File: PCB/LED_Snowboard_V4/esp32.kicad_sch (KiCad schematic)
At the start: 28 parts

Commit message: makerfaire
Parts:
- TP1, TP2, TP3, TP4, TP5: footprint (none) -> TestPoint:TestPoint_Pad_3.0x3.0mm
- TP10, TP11, TP12, TP13, TP14, TP15, TP16, TP17, TP18, TP19, TP20, TP21, TP22, TP23, TP24, TP25, TP26, TP27, TP6, TP7, TP8, TP9: footprint (none) -> TestPoint:TestPoint_Pad_D1.5mm
- U1: footprint (none) -> MicroControllers:MODULE_ESP32_DEVKIT_V1
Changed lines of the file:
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@@
       (effects (font (size 1.27 1.27)))
     )
-    (property "Footprint" "" (at 31.75 181.61 0)
+    (property "Footprint" "TestPoint:TestPoint_Pad_D1.5mm" (at 31.75 181.61 0)
       (effects (font (size 1.27 1.27)) hide)
     )
@@
       (effects (font (size 1.27 1.27)))
     )
-    (property "Footprint" "" (at 31.75 34.29 0)
+    (property "Footprint" "TestPoint:TestPoint_Pad_3.0x3.0mm" (at 31.75 34.29 0)
       (effects (font (size 1.27 1.27)) hide)
     )
@@
       (effects (font (size 1.27 1.27)))
     )
-    (property "Footprint" "" (at 143.51 111.76 0)
+    (property "Footprint" "MicroControllers:MODULE_ESP32_DEVKIT_V1" (at 143.51 111.76 0)
       (effects (font (size 1.27 1.27)) hide)
     )
@@
       (effects (font (size 1.27 1.27)))
     )
-    (property "Footprint" "" (at 31.75 186.69 0)
+    (property "Footprint" "TestPoint:TestPoint_Pad_D1.5mm" (at 31.75 186.69 0)
       (effects (font (size 1.27 1.27)) hide)
     )
@@
       (effects (font (size 1.27 1.27)))
     )
-    (property "Footprint" "" (at 31.75 116.84 0)
+    (property "Footprint" "TestPoint:TestPoint_Pad_D1.5mm" (at 31.75 116.84 0)
       (effects (font (size 1.27 1.27)) hide)
     )
@@
       (effects (font (size 1.27 1.27)))
     )
-    (property "Footprint" "" (at 31.75 167.64 0)
+    (property "Footprint" "TestPoint:TestPoint_Pad_D1.5mm" (at 31.75 167.64 0)
       (effects (font (size 1.27 1.27)) hide)
     )
@@
       (effects (font (size 1.27 1.27)))
     )
-    (property "Footprint" "" (at 31.75 138.43 0)
+    (property "Footprint" "TestPoint:TestPoint_Pad_D1.5mm" (at 31.75 138.43 0)
       (effects (font (size 1.27 1.27)) hide)
     )
@@
       (effects (font (size 1.27 1.27)))
     )
-    (property "Footprint" "" (at 31.75 162.56 0)
+    (property "Footprint" "TestPoint:TestPoint_Pad_D1.5mm" (at 31.75 162.56 0)
       (effects (font (size 1.27 1.27)) hide)
     )
@@
       (effects (font (size 1.27 1.27)))
     )
-    (property "Footprint" "" (at 31.75 60.96 0)
+    (property "Footprint" "TestPoint:TestPoint_Pad_D1.5mm" (at 31.75 60.96 0)
       (effects (font (size 1.27 1.27)) hide)
     )
@@
       (effects (font (size 1.27 1.27)))
     )
-    (property "Footprint" "" (at 31.75 29.21 0)
+    (property "Footprint" "TestPoint:TestPoint_Pad_3.0x3.0mm" (at 31.75 29.21 0)
       (effects (font (size 1.27 1.27)) hide)
     )
@@
       (effects (font (size 1.27 1.27)))
     )
-    (property "Footprint" "" (at 31.75 39.37 0)
+    (property "Footprint" "TestPoint:TestPoint_Pad_3.0x3.0mm" (at 31.75 39.37 0)
       (effects (font (size 1.27 1.27)) hide)
     )
@@
       (effects (font (size 1.27 1.27)))
     )
-    (property "Footprint" "" (at 31.75 24.13 0)
+    (property "Footprint" "TestPoint:TestPoint_Pad_3.0x3.0mm" (at 31.75 24.13 0)
       (effects (font (size 1.27 1.27)) hide)
     )
@@
       (effects (font (size 1.27 1.27)))
     )
-    (property "Footprint" "" (at 31.75 133.35 0)
+    (property "Footprint" "TestPoint:TestPoint_Pad_D1.5mm" (at 31.75 133.35 0)
       (effects (font (size 1.27 1.27)) hide)
     )
@@
       (effects (font (size 1.27 1.27)))
     )
-    (property "Footprint" "" (at 31.75 105.41 0)
+    (property "Footprint" "TestPoint:TestPoint_Pad_D1.5mm" (at 31.75 105.41 0)
       (effects (font (size 1.27 1.27)) hide)
     )
@@
       (effects (font (size 1.27 1.27)))
     )
-    (property "Footprint" "" (at 31.75 86.36 0)
+    (property "Footprint" "TestPoint:TestPoint_Pad_D1.5mm" (at 31.75 86.36 0)
       (effects (font (size 1.27 1.27)) hide)
     )
@@
       (effects (font (size 1.27 1.27)))
     )
-    (property "Footprint" "" (at 31.75 76.2 0)
+    (property "Footprint" "TestPoint:TestPoint_Pad_D1.5mm" (at 31.75 76.2 0)
       (effects (font (size 1.27 1.27)) hide)
     )
@@
       (effects (font (size 1.27 1.27)))
     )
-    (property "Footprint" "" (at 31.75 100.33 0)
+    (property "Footprint" "TestPoint:TestPoint_Pad_D1.5mm" (at 31.75 100.33 0)
       (effects (font (size 1.27 1.27)) hide)
     )
@@
       (effects (font (size 1.27 1.27)))
     )
-    (property "Footprint" "" (at 31.75 50.8 0)
+    (property "Footprint" "TestPoint:TestPoint_Pad_D1.5mm" (at 31.75 50.8 0)
       (effects (font (size 1.27 1.27)) hide)
     )
@@
       (effects (font (size 1.27 1.27)))
     )
-    (property "Footprint" "" (at 31.75 157.48 0)
+    (property "Footprint" "TestPoint:TestPoint_Pad_D1.5mm" (at 31.75 157.48 0)
       (effects (font (size 1.27 1.27)) hide)
     )
@@
       (effects (font (size 1.27 1.27)))
     )
-    (property "Footprint" "" (at 31.75 19.05 0)
+    (property "Footprint" "TestPoint:TestPoint_Pad_3.0x3.0mm" (at 31.75 19.05 0)
       (effects (font (size 1.27 1.27)) hide)
     )
@@
       (effects (font (size 1.27 1.27)))
     )
-    (property "Footprint" "" (at 31.75 121.92 0)
+    (property "Footprint" "TestPoint:TestPoint_Pad_D1.5mm" (at 31.75 121.92 0)
       (effects (font (size 1.27 1.27)) hide)
     )
@@
       (effects (font (size 1.27 1.27)))
     )
-    (property "Footprint" "" (at 31.75 66.04 0)
+    (property "Footprint" "TestPoint:TestPoint_Pad_D1.5mm" (at 31.75 66.04 0)
       (effects (font (size 1.27 1.27)) hide)
     )
@@
       (effects (font (size 1.27 1.27)))
     )
-    (property "Footprint" "" (at 31.75 55.88 0)
+    (property "Footprint" "TestPoint:TestPoint_Pad_D1.5mm" (at 31.75 55.88 0)
       (effects (font (size 1.27 1.27)) hide)
     )
@@
       (effects (font (size 1.27 1.27)))
     )
-    (property "Footprint" "" (at 31.75 91.44 0)
+    (property "Footprint" "TestPoint:TestPoint_Pad_D1.5mm" (at 31.75 91.44 0)
       (effects (font (size 1.27 1.27)) hide)
     )
@@
       (effects (font (size 1.27 1.27)))
     )
-    (property "Footprint" "" (at 31.75 143.51 0)
+    (property "Footprint" "TestPoint:TestPoint_Pad_D1.5mm" (at 31.75 143.51 0)
       (effects (font (size 1.27 1.27)) hide)
     )
@@
       (effects (font (size 1.27 1.27)))
     )
-    (property "Footprint" "" (at 31.75 176.53 0)
+    (property "Footprint" "TestPoint:TestPoint_Pad_D1.5mm" (at 31.75 176.53 0)
       (effects (font (size 1.27 1.27)) hide)
     )
@@
       (effects (font (size 1.27 1.27)))
     )
-    (property "Footprint" "" (at 31.75 148.59 0)
+    (property "Footprint" "TestPoint:TestPoint_Pad_D1.5mm" (at 31.75 148.59 0)
       (effects (font (size 1.27 1.27)) hide)
     )
@@
       (effects (font (size 1.27 1.27)))
     )
-    (property "Footprint" "" (at 31.75 81.28 0)
-      (effects (font (size 1.27 1.27)) hide)
-    )
+    (property "Footprint" "TestPoint:TestPoint_Pad_D1.5mm" (at 31.75 81.28 0)
+      (effects (font (size 1.27 1.27)) hide)
+    )

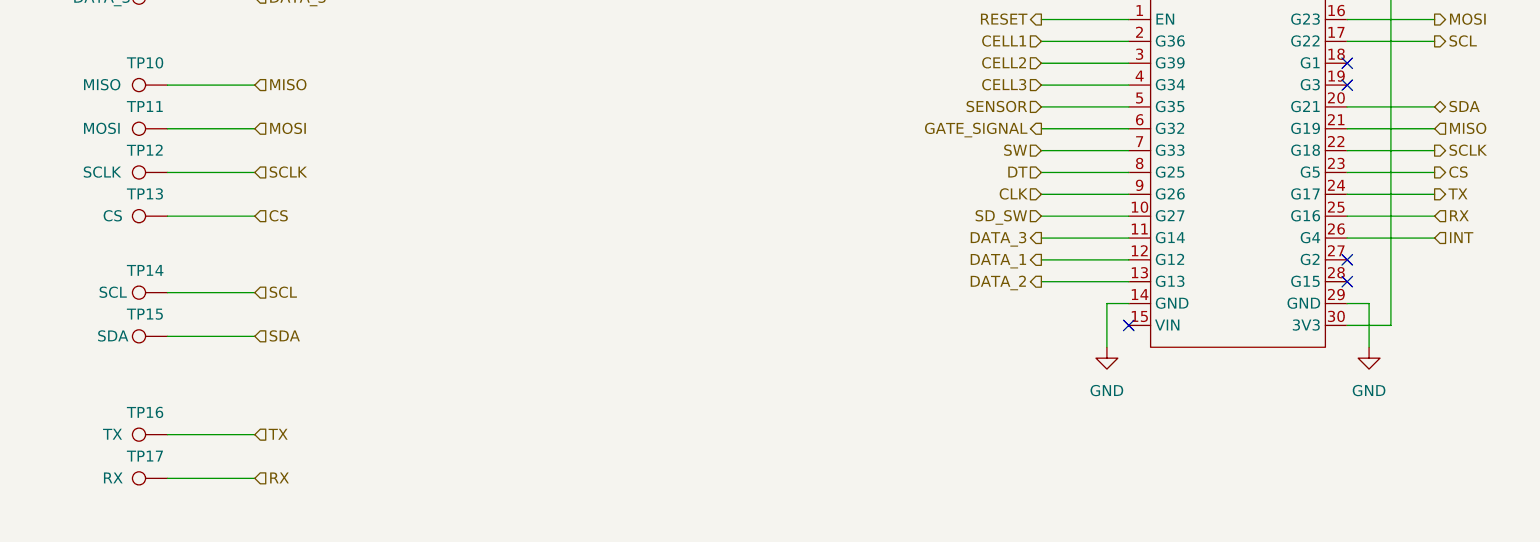
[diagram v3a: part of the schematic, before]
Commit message: Added Ram
Added Ram. need to finish DRC checks
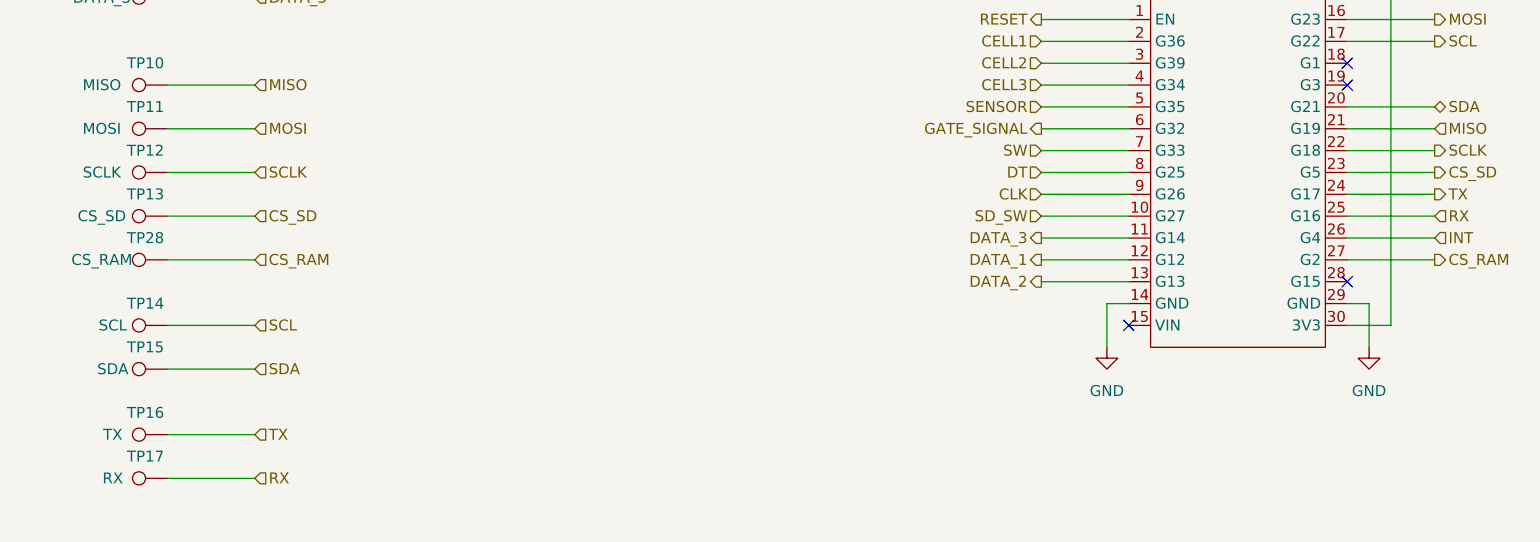
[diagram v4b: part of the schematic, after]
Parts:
- added TP28: CS_RAM, TestPoint:TestPoint_Pad_D1.5mm, symbol Connector:TestPoint
- TP13: value CS -> CS_SD
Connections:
- net CS_RAM: now reaches U1.27 (G2)
- net CS_RAM: now also TP28.1
- net CS renamed CS_SD
- no-connect marks 5 -> 4
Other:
- moved on the sheet: TP14, TP15
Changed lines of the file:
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@@
   )
   (no_connect (at 143.51 109.22))
-  (no_connect (at 168.91 101.6))
   (no_connect (at 168.91 81.28))
   (no_connect (at 168.91 104.14))
@@
     (stroke (width 0) (type default))
   )
-  (wire (pts (xy 31.75 110.49) (xy 41.91 110.49))
+  (wire (pts (xy 31.75 114.3) (xy 41.91 114.3))
     (stroke (width 0) (type default))
   )
@@
     (stroke (width 0) (type default))
   )
+  (wire (pts (xy 168.91 101.6) (xy 179.07 101.6))
+    (stroke (width 0) (type default))
+  )
   (wire (pts (xy 168.91 99.06) (xy 179.07 99.06))
     (stroke (width 0) (type default))
@@
     (stroke (width 0) (type default))
   )
-  (wire (pts (xy 31.75 105.41) (xy 41.91 105.41))
+  (wire (pts (xy 31.75 109.22) (xy 41.91 109.22))
     (stroke (width 0) (type default))
   )
   (wire (pts (xy 133.35 96.52) (xy 143.51 96.52))
+    (stroke (width 0) (type default))
+  )
+  (wire (pts (xy 31.75 101.6) (xy 41.91 101.6))
     (stroke (width 0) (type default))
   )
@@
     (effects (font (size 1.27 1.27)) (justify right))
   )
-  (hierarchical_label "SDA" (shape input) (at 41.91 110.49 0) (fields_autoplaced)
+  (hierarchical_label "SDA" (shape input) (at 41.91 114.3 0) (fields_autoplaced)
     (effects (font (size 1.27 1.27)) (justify left))
   )
@@
     (effects (font (size 1.27 1.27)) (justify left))
   )
-  (hierarchical_label "SCL" (shape input) (at 41.91 105.41 0) (fields_autoplaced)
+  (hierarchical_label "SCL" (shape input) (at 41.91 109.22 0) (fields_autoplaced)
     (effects (font (size 1.27 1.27)) (justify left))
   )
   (hierarchical_label "DATA_2" (shape input) (at 41.91 66.04 0) (fields_autoplaced)
+    (effects (font (size 1.27 1.27)) (justify left))
+  )
+  (hierarchical_label "CS_RAM" (shape output) (at 179.07 101.6 0) (fields_autoplaced)
     (effects (font (size 1.27 1.27)) (justify left))
   )
@@
     (effects (font (size 1.27 1.27)) (justify left))
   )
-  (hierarchical_label "CS" (shape input) (at 41.91 96.52 0) (fields_autoplaced)
+  (hierarchical_label "CS_SD" (shape input) (at 41.91 96.52 0) (fields_autoplaced)
     (effects (font (size 1.27 1.27)) (justify left))
   )
@@
     (effects (font (size 1.27 1.27)) (justify left))
   )
+  (hierarchical_label "CS_RAM" (shape input) (at 41.91 101.6 0) (fields_autoplaced)
+    (effects (font (size 1.27 1.27)) (justify left))
+  )
   (hierarchical_label "MOSI" (shape input) (at 41.91 86.36 0) (fields_autoplaced)
     (effects (font (size 1.27 1.27)) (justify left))
@@
     (effects (font (size 1.27 1.27)) (justify left))
   )
-  (hierarchical_label "CS" (shape output) (at 179.07 91.44 0) (fields_autoplaced)
+  (hierarchical_label "CS_SD" (shape output) (at 179.07 91.44 0) (fields_autoplaced)
     (effects (font (size 1.27 1.27)) (justify left))
   )
@@
         (path "/69eedaaa-0c0b-424a-87de-b98a25a250e0/1c15da28-0360-4802-9478-e55dfae7ff35"
           (reference "TP63") (unit 1)
+        )
+      )
+    )
+  )
+  (symbol (lib_id "Connector:TestPoint") (at 31.75 101.6 90) (unit 1)
+    (in_bom yes) (on_board yes) (dnp no)
+    (property "Reference" "TP28" (at 29.21 99.06 90)
+      (effects (font (size 1.27 1.27)))
+    )
+    (property "Value" "CS_RAM" (at 24.13 101.6 90)
+      (effects (font (size 1.27 1.27)))
+    )
+    (property "Footprint" "TestPoint:TestPoint_Pad_D1.5mm" (at 31.75 96.52 0)
+      (effects (font (size 1.27 1.27)) hide)
+    )
+    (property "Datasheet" "~" (at 31.75 96.52 0)
+      (effects (font (size 1.27 1.27)) hide)
+    )
+    (pin "1")
+    (instances
+      (project "LED_Snowboard_V4"
+        (path "/69eedaaa-0c0b-424a-87de-b98a25a250e0/e9bdeec5-f2c1-4c3a-b433-37b4e9dce032"
+          (reference "TP28") (unit 1)
+        )
+        (path "/69eedaaa-0c0b-424a-87de-b98a25a250e0/609d0ec3-3d5e-48f8-8437-e8dde642f153"
+          (reference "TP22") (unit 1)
+        )
+        (path "/69eedaaa-0c0b-424a-87de-b98a25a250e0/1c15da28-0360-4802-9478-e55dfae7ff35"
+          (reference "TP24") (unit 1)
         )
       )
@@
     )
   )
-  (symbol (lib_id "Connector:TestPoint") (at 31.75 110.49 90) (unit 1)
-    (in_bom yes) (on_board yes) (dnp no)
-    (property "Reference" "TP15" (at 29.21 107.95 90)
-      (effects (font (size 1.27 1.27)))
-    )
-    (property "Value" "SDA" (at 25.4 110.49 90)
-      (effects (font (size 1.27 1.27)))
-    )
-    (property "Footprint" "TestPoint:TestPoint_Pad_D1.5mm" (at 31.75 105.41 0)
-      (effects (font (size 1.27 1.27)) hide)
-    )
-    (property "Datasheet" "~" (at 31.75 105.41 0)
+  (symbol (lib_id "Connector:TestPoint") (at 31.75 114.3 90) (unit 1)
+    (in_bom yes) (on_board yes) (dnp no)
+    (property "Reference" "TP15" (at 29.21 111.76 90)
+      (effects (font (size 1.27 1.27)))
+    )
+    (property "Value" "SDA" (at 25.4 114.3 90)
+      (effects (font (size 1.27 1.27)))
+    )
+    (property "Footprint" "TestPoint:TestPoint_Pad_D1.5mm" (at 31.75 109.22 0)
+      (effects (font (size 1.27 1.27)) hide)
+    )
+    (property "Datasheet" "~" (at 31.75 109.22 0)
       (effects (font (size 1.27 1.27)) hide)
     )
@@
     )
   )
-  (symbol (lib_id "Connector:TestPoint") (at 31.75 105.41 90) (unit 1)
-    (in_bom yes) (on_board yes) (dnp no)
-    (property "Reference" "TP14" (at 29.21 102.87 90)
-      (effects (font (size 1.27 1.27)))
-    )
-    (property "Value" "SCL" (at 25.4 105.41 90)
-      (effects (font (size 1.27 1.27)))
-    )
-    (property "Footprint" "TestPoint:TestPoint_Pad_D1.5mm" (at 31.75 100.33 0)
-      (effects (font (size 1.27 1.27)) hide)
-    )
-    (property "Datasheet" "~" (at 31.75 100.33 0)
+  (symbol (lib_id "Connector:TestPoint") (at 31.75 109.22 90) (unit 1)
+    (in_bom yes) (on_board yes) (dnp no)
+    (property "Reference" "TP14" (at 29.21 106.68 90)
+      (effects (font (size 1.27 1.27)))
+    )
+    (property "Value" "SCL" (at 25.4 109.22 90)
+      (effects (font (size 1.27 1.27)))
+    )
+    (property "Footprint" "TestPoint:TestPoint_Pad_D1.5mm" (at 31.75 104.14 0)
+      (effects (font (size 1.27 1.27)) hide)
+    )
+    (property "Datasheet" "~" (at 31.75 104.14 0)
       (effects (font (size 1.27 1.27)) hide)
     )
@@
       (effects (font (size 1.27 1.27)))
     )
-    (property "Value" "CS" (at 25.4 96.52 90)
-      (effects (font (size 1.27 1.27)))
-    )
+    (property "Value" "CS_SD" (at 24.13 96.52 90)
+      (effects (font (size 1.27 1.27)))
+    )
